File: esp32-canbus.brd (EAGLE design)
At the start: 50.2 x 49.5 mm, 59 parts, among them J1 PRPC006DBAN-M71RC, J2 USB-MICROB-3, U1 ESP32, U10 TPS62172DSGR, U3 MCP2515T-I/ML, U4 MCP2515T-I/ML, U5 MCP2515T-I/ML, U6 MCP2558FDT-H/MNY, U7 MCP2558FDT-H/MNY, U8 MCP2558FDT-H/MNY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

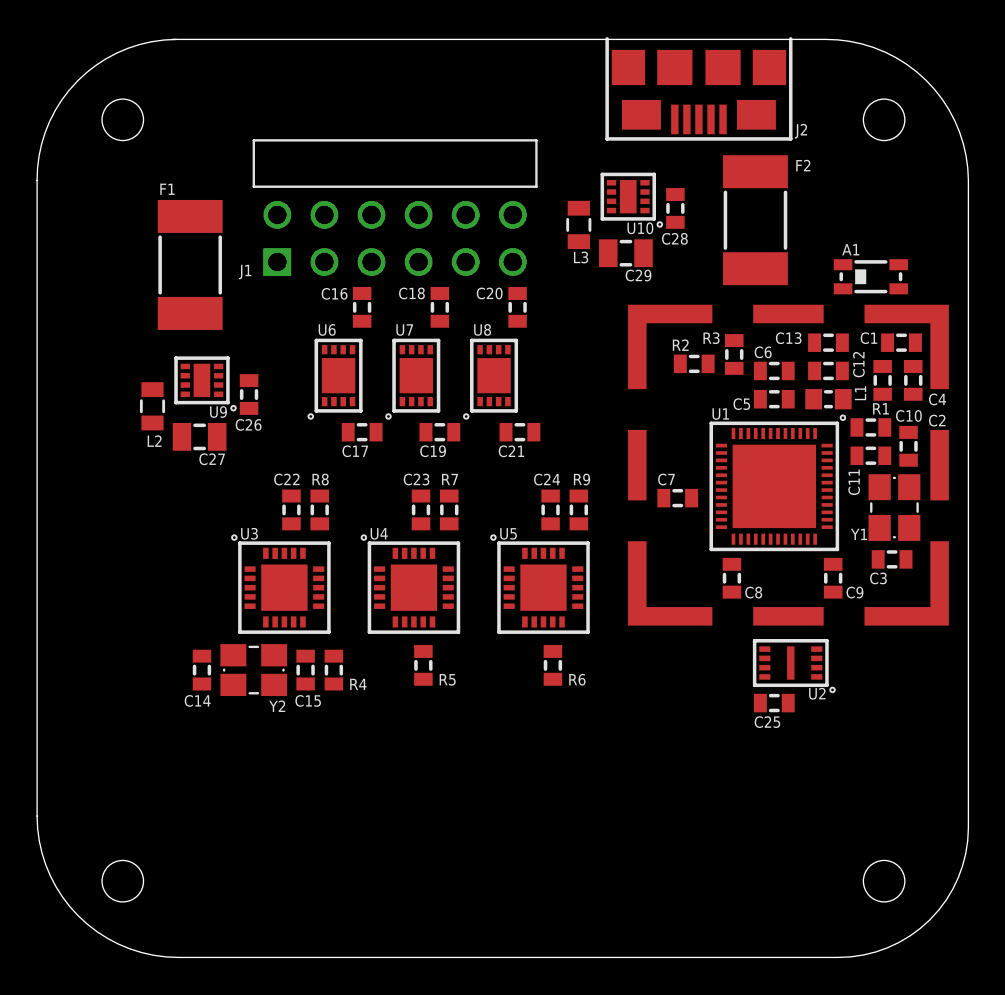
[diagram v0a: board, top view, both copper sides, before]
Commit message: Update board
Rout mode of the board and a few edits in the schematic
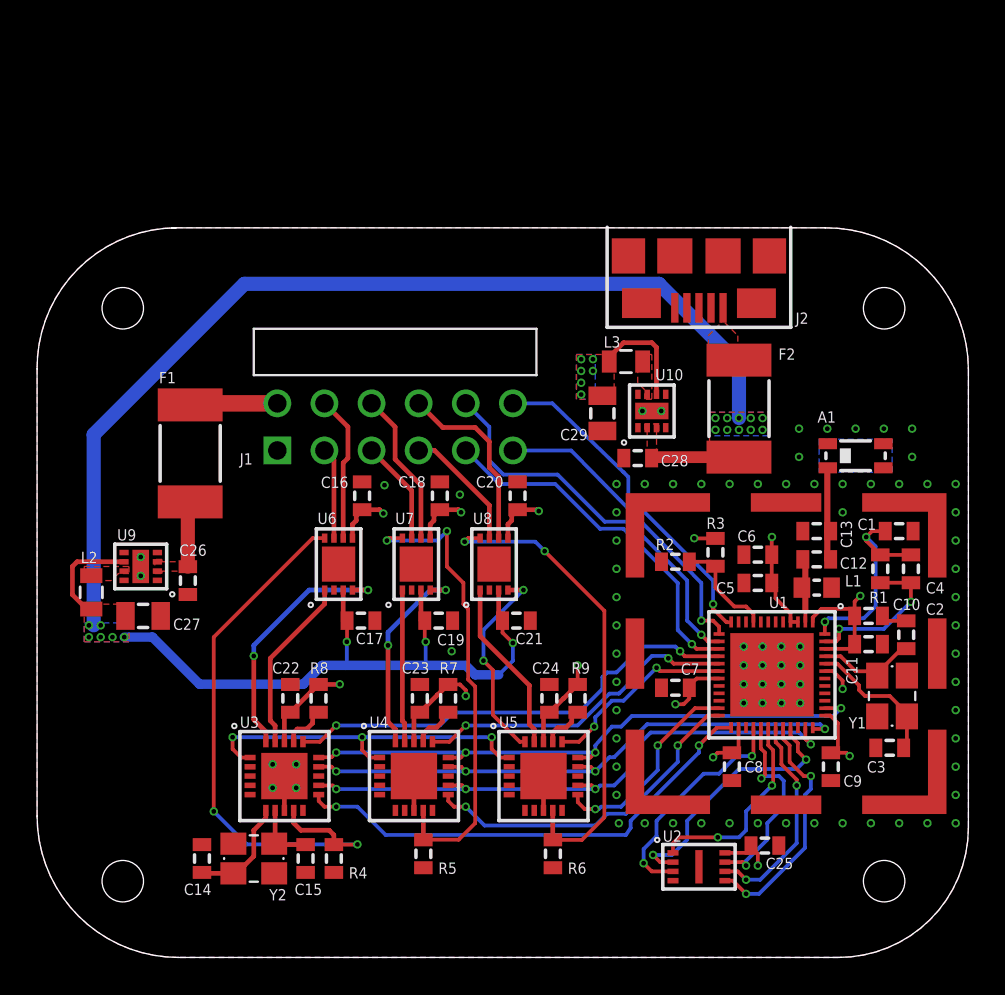
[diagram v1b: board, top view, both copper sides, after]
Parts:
- moved C28 13.6 mm to (32.4, 26.9), turned to 180 degrees
- moved U2 12.1 mm to (35.7, 4.89), turned to 0 degrees
- moved U10 11.6 mm to (33.1, 29.5), turned to 90 degrees
- moved R2 10.7 mm to (34.4, 21.3), turned to 0 degrees
- moved R3 10.7 mm to (36.6, 21.8), turned to 90 degrees
- moved C26 10.6 mm to (8.13, 20.3)
- moved L2 10.6 mm to (2.92, 19.7)
- moved U9 10.6 mm to (5.59, 21.1)
- moved C7 10.2 mm to (34.4, 14.5)
- moved F2 10.2 mm to (37.8, 29.6)
- moved C12 10.2 mm to (42.0, 21.5)
- moved C13 10.2 mm to (42.0, 23.0)
- moved L1 10.2 mm to (42.0, 19.9)
- moved C21 10.2 mm to (25.8, 18.2)
- moved Y1 10.2 mm to (46.1, 14.1)
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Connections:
- net !INT0: now also U1.25; no longer U1.23
- net !INT2: now also U1.23; no longer U1.25
- net A0: now also J1.12; no longer J1.9
- net A1: now also J1.11; no longer J1.10
- net A2: now also J1.10; no longer J1.11
- net A3: now also J1.9; no longer J1.12
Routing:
- net 5V: track 0.00 -> 99.4 mm, vias 0 -> 19
- net 3.3V: track 0.00 -> 58.9 mm, vias 0 -> 20
- net MISO: track 0.00 -> 32.5 mm, vias 0 -> 4
- net SCK: track 0.00 -> 31.7 mm, vias 0 -> 4
- net MOSI: track 0.00 -> 31.4 mm, vias 0 -> 4
- net N$10: track 0.00 -> 31.0 mm, vias 0 -> 2
- net GND: track 0.00 -> 28.0 mm, vias 0 -> 83
- net !INT0: track 0.00 -> 26.2 mm, vias 0 -> 2
- net N$16: track 0.00 -> 26.0 mm, vias 0 -> 2
- net N$13: track 0.00 -> 25.5 mm, vias 0 -> 2
- net !CS0: track 0.00 -> 25.2 mm, vias 0 -> 2
- net A2: track 0.00 -> 21.3 mm, vias 0 -> 1
- net A3: track 0.00 -> 19.6 mm, vias 0 -> 1
- net CAN_CLK: track 0.00 -> 19.3 mm, vias 0 -> 3
- net !INT1: track 0.00 -> 18.5 mm, vias 0 -> 2
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- added copper zone on layer 1, net 12V
- added copper zone on layer 1, net 3.3V
- added copper zone on layer 15, net 3.3V
- added copper zone on layer 16, net 3.3V
- added copper zone on layer 1, net 5V
- added copper zone on layer 16, net 5V
- added copper zone on layer 1, net GND
- added copper zone on layer 16, net GND
- added copper zone on layer 2, net GND
- added copper zone on layer 15, net N$22
- added copper zone on layer 16, net N$22
- added copper zone on layer 2, net N$22
- added copper zone on layer 1, net N$23
- added copper zone on layer 1, net N$24
- added copper zone on layer 1, net N$25
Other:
- board size 50.2 x 49.5 mm -> 50.2 x 39.3 mm

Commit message: Update board
Finish board layou, tweak a few things in schematic, and add documents
(ger ber files, pdf schematic)
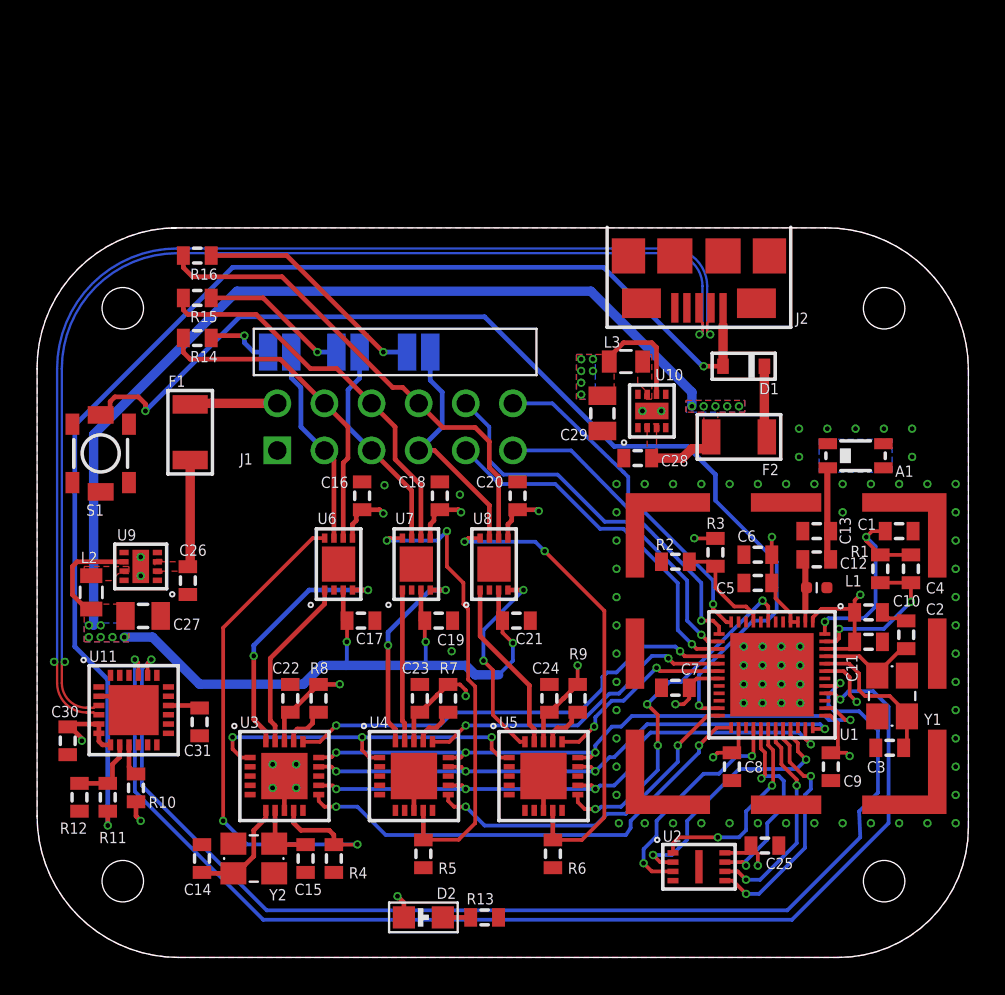
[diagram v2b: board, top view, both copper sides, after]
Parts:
- added C30, C31: 0.1uF, Passives:0603-CAP
- added D1: NSR0530HT1G, ON Semiconductor:SOD323
- added D2: LH R974-LP-1, Passives:0805-LED
- added JUMPER1, JUMPER2, JUMPER3: JUMPER-NO, Passives:JUMPER-NO
- added R10, R11, R12: 10k, Passives:0603-CAP
- added R13: 1k, Passives:0603-CAP
- added R14, R15, R16: 120, Passives:0603-CAP
- added S1: TACTILE-SMD2, Passives:PTS820-J15M-SMTR-LFS
- added U11: CP2104-F03-GM, Silicon Labs:QFN-24-4X4
- C14, C2: value 18pF -> 10pF
- C15, C3: value 18pFF -> 10pF
- F1, F2: value (none) -> 0ZCJ0050AF2E; device Passives:1812-PTC -> Passives:1206-PTC
- J2: value USB-MICROB-3 -> 10118192-0001LF
- L1: device Passives:0603-FERRITE -> Passives:0402-INDUCTOR
- SH1: value RF-SHIELD -> BMI-S-102
- U2: value (none) -> SST26WF080BT-104I/NP
- moved F2 1.52 mm to (37.8, 28.1), turned to 0 degrees
- moved F1 1.14 mm to (8.26, 28.3), turned to 90 degrees
- moved C10 0.19 mm to (44.8, 18.6)
- moved C11 0.13 mm to (44.8, 17.0)
- renumbered U$1 to SH1
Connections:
- new net D_N: J2.2, U11.4
- new net D_P: J2.3, U11.3
- new net N$27: R10.1, U11.9
- new net N$28: D1.C, F2.P$1
- new net N$29: D2.C, R13.2
- new net N$31: JUMPER1.P$2, R14.1
- new net N$32: C31.1, U11.16
- new net N$34: JUMPER2.P$2, R15.1
- new net N$35: JUMPER3.P$2, R16.1
- new net PROGRAM: S1.2, U1.23
- new net VBUS: D1.A, J2.1, R11.2
- net !INT2: now also U1.7; no longer U1.23
- net 12V: now also F1.P$2; no longer F1.2
- net 3.3V: now also C30.1, D2.A, R10.2, U11.5, U11.6, U11.7
- net 5V: now also F2.P$2; no longer F2.2
- net CAN1H: now also JUMPER1.P$1
- net CAN1L: now also R14.2
- net CAN2H: now also JUMPER2.P$1
- net CAN2L: now also R15.2
- net CAN3H: now also JUMPER3.P$1
- net CAN3L: now also R16.2
- net GND: now also C30.2, C31.2, L1.1, R12.1, R13.1, S1.1, U11.2, U11.PAD; no longer L1.P$1
- net N$23: now also R11.1, R12.2, U11.8; no longer F2.1, J2.1
- net N$26: now also F1.P$1; no longer F1.1
- net N$6: now also L1.2; no longer L1.P$2
- net RX: now also U11.21
- net TX: now also U11.20
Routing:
- net VBUS: track 0.00 -> 66.9 mm, vias 0 -> 2
- net RX: track 0.00 -> 64.1 mm, vias 0 -> 2
- net D_N: track 0.00 -> 63.3 mm, vias 0 -> 2
- net TX: track 0.00 -> 62.9 mm, vias 0 -> 2
- net D_P: track 0.00 -> 62.2 mm, vias 0 -> 2
- net PROGRAM: track 0.00 -> 57.3 mm, vias 0 -> 2
- net CAN3L: track 10.1 -> 26.4 mm
- net CAN2L: track 8.37 -> 21.3 mm
- net N$35: track 0.00 -> 12.7 mm, vias 0 -> 1
- net CAN1L: track 7.90 -> 17.4 mm
- net 3.3V: track 58.9 -> 67.5 mm, vias 20 -> 23
- net !INT2: track 11.2 -> 19.3 mm, vias 2 -> 4
- net N$34: track 0.00 -> 7.96 mm, vias 0 -> 1
- net CAN3H: track 6.81 -> 12.9 mm
- net CAN2H: track 5.62 -> 11.7 mm
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- removed copper zone on layer 1, net N$23
